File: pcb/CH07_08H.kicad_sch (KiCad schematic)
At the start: 10 parts

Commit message: Corrections to the coax driver
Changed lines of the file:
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@@
     (effects (font (size 1.27 1.27)) (justify right))
   )
-  (symbol (lib_id "Transistor_BJT:BC856BS") (at 106.68 52.07 0) (mirror x)
+  (symbol (lib_id "Transistor_BJT:BC856BS") (at 106.68 52.07 0) (mirror x) (unit 1)
     (in_bom yes) (on_board yes)
     (property "Reference" "Q?" (id 0) (at 111.506 53.2384 0)
@@
     (pin "6")
   )
-  (symbol (lib_id "Transistor_BJT:BC856BS") (at 106.68 114.3 0) (mirror x)
+  (symbol (lib_id "Transistor_BJT:BC856BS") (at 106.68 114.3 0) (mirror x) (unit 1)
     (in_bom yes) (on_board yes)
     (property "Reference" "Q?" (id 0) (at 111.506 115.4684 0)
@@
       (effects (font (size 1.27 1.27)) hide)
     )
-    (pin "3")
-    (pin "4")
-    (pin "5")
+    (pin "1")
+    (pin "2")
+    (pin "6")
   )
-  (symbol (lib_id "Device:R") (at 115.57 69.85 0)
+  (symbol (lib_id "Device:R") (at 115.57 69.85 0) (unit 1)
     (in_bom yes) (on_board yes)
     (property "Reference" "R?" (id 0) (at 117.348 68.6816 0)
@@
     (pin "2")
   )
-  (symbol (lib_id "power:GND") (at 115.57 86.36 0)
+  (symbol (lib_id "power:GND") (at 115.57 86.36 0) (unit 1)
     (in_bom yes) (on_board yes)
     (property "Reference" "#PWR?" (id 0) (at 115.57 92.71 0)
@@
     (pin "1")
   )
-  (symbol (lib_id "Device:R") (at 115.57 80.01 0)
+  (symbol (lib_id "Device:R") (at 115.57 80.01 0) (unit 1)
     (in_bom yes) (on_board yes)
     (property "Reference" "R?" (id 0) (at 117.348 78.8416 0)
@@
     (pin "2")
   )
-  (symbol (lib_id "Device:R") (at 114.3 132.08 0)
+  (symbol (lib_id "Device:R") (at 114.3 132.08 0) (unit 1)
     (in_bom yes) (on_board yes)
     (property "Reference" "R?" (id 0) (at 116.078 130.9116 0)
@@
     (pin "2")
   )
-  (symbol (lib_id "power:GND") (at 114.3 149.86 0)
+  (symbol (lib_id "power:GND") (at 114.3 149.86 0) (unit 1)
     (in_bom yes) (on_board yes)
     (property "Reference" "#PWR?" (id 0) (at 114.3 156.21 0)
@@
     (pin "1")
   )
-  (symbol (lib_id "Device:R") (at 114.3 143.51 0)
+  (symbol (lib_id "Device:R") (at 114.3 143.51 0) (unit 1)
     (in_bom yes) (on_board yes)
     (property "Reference" "R?" (id 0) (at 116.078 142.3416 0)
@@
     (pin "2")
   )
-  (symbol (lib_id "Connector:Conn_Coaxial") (at 115.57 59.69 0)
+  (symbol (lib_id "Connector:Conn_Coaxial") (at 115.57 59.69 0) (unit 1)
     (in_bom yes) (on_board yes)
     (property "Reference" "J?" (id 0) (at 118.11 60.325 0)
@@
     (pin "2")
   )
-  (symbol (lib_id "Device:R") (at 93.98 52.07 270)
+  (symbol (lib_id "Device:R") (at 93.98 52.07 270) (unit 1)
     (in_bom yes) (on_board yes)
     (property "Reference" "R?" (id 0) (at 93.98 46.8122 90))
@@
     (pin "2")
   )
-  (symbol (lib_id "Connector:Conn_Coaxial") (at 114.3 121.92 0)
+  (symbol (lib_id "Connector:Conn_Coaxial") (at 114.3 121.92 0) (unit 1)
     (in_bom yes) (on_board yes)
     (property "Reference" "J?" (id 0) (at 116.84 122.555 0)
@@
     (pin "2")
   )
-  (symbol (lib_id "Device:R") (at 93.98 114.3 270)
+  (symbol (lib_id "Device:R") (at 93.98 114.3 270) (unit 1)
     (in_bom yes) (on_board yes)
     (property "Reference" "R?" (id 0) (at 93.98 109.0422 90))

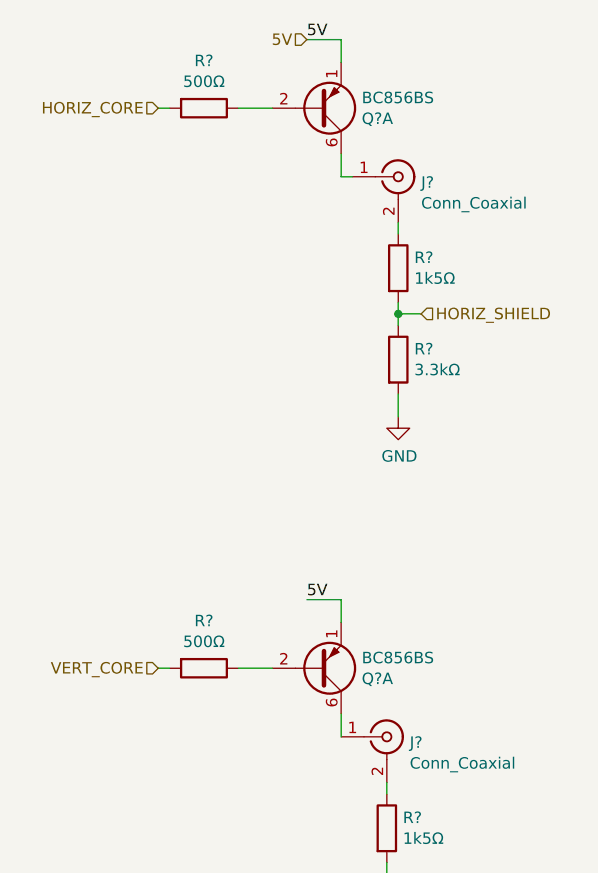
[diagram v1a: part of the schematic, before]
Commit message: Shift register updates - changes the driver from pnp to npn
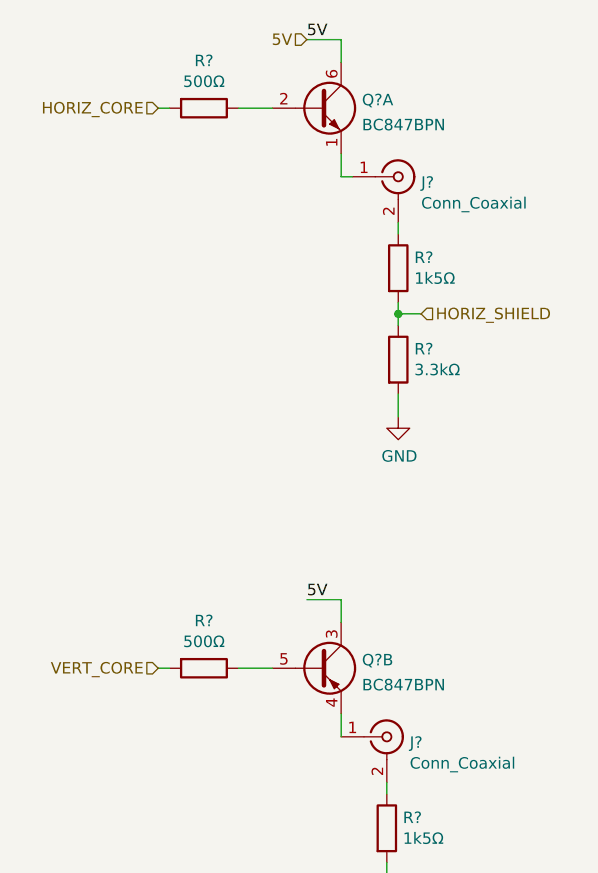
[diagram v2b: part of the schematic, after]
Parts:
- removed Q? (x2): BC856BS, Package_TO_SOT_SMD:SOT-363_SC-70-6, symbol Transistor_BJT:BC856BS
- added Q? (x2): BC847BPN, Package_TO_SOT_SMD:SOT-363_SC-70-6, symbol Transistor_BJT:BC847BPN
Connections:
- net 5V: now also Q?.3 (C2), Q?.6 (C1)
- net at R?.1: now also Q?.2 (B1)
- net at J?.1 (In): now also Q?.1 (E1)
- net at R?.1: now also Q?.5 (B2)
- net at J?.1 (In): now also Q?.4 (E2)
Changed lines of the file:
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@@
     (effects (font (size 1.27 1.27)) (justify right))
-  )
-  (symbol (lib_id "Transistor_BJT:BC856BS") (at 106.68 52.07 0) (mirror x) (unit 1)
-    (in_bom yes) (on_board yes)
-    (property "Reference" "Q?" (id 0) (at 111.506 53.2384 0)
-      (effects (font (size 1.27 1.27)) (justify left))
-    )
-    (property "Value" "BC856BS" (id 1) (at 111.506 50.927 0)
-      (effects (font (size 1.27 1.27)) (justify left))
-    )
-    (property "Footprint" "Package_TO_SOT_SMD:SOT-363_SC-70-6" (id 2) (at 111.76 54.61 0)
-      (effects (font (size 1.27 1.27)) hide)
-    )
-    (property "Datasheet" "https://assets.nexperia.com/documents/data-sheet/BC856BS.pdf" (id 3) (at 106.68 52.07 0)
-      (effects (font (size 1.27 1.27)) hide)
-    )
-    (pin "1")
-    (pin "2")
-    (pin "6")
-  )
-  (symbol (lib_id "Transistor_BJT:BC856BS") (at 106.68 114.3 0) (mirror x) (unit 1)
-    (in_bom yes) (on_board yes)
-    (property "Reference" "Q?" (id 0) (at 111.506 115.4684 0)
-      (effects (font (size 1.27 1.27)) (justify left))
-    )
-    (property "Value" "BC856BS" (id 1) (at 111.506 113.157 0)
-      (effects (font (size 1.27 1.27)) (justify left))
-    )
-    (property "Footprint" "Package_TO_SOT_SMD:SOT-363_SC-70-6" (id 2) (at 111.76 116.84 0)
-      (effects (font (size 1.27 1.27)) hide)
-    )
-    (property "Datasheet" "https://assets.nexperia.com/documents/data-sheet/BC856BS.pdf" (id 3) (at 106.68 114.3 0)
-      (effects (font (size 1.27 1.27)) hide)
-    )
-    (pin "1")
-    (pin "2")
-    (pin "6")
   )
   (symbol (lib_id "Device:R") (at 115.57 69.85 0) (unit 1)
@@
     (pin "2")
   )
+  (symbol (lib_id "Transistor_BJT:BC847BPN") (at 106.68 114.3 0) (unit 2)
+    (in_bom yes) (on_board yes) (fields_autoplaced)
+    (property "Reference" "Q?" (id 0) (at 111.5314 113.3915 0)
+      (effects (font (size 1.27 1.27)) (justify left))
+    )
+    (property "Value" "BC847BPN" (id 1) (at 111.5314 116.1666 0)
+      (effects (font (size 1.27 1.27)) (justify left))
+    )
+    (property "Footprint" "Package_TO_SOT_SMD:SOT-363_SC-70-6" (id 2) (at 111.76 111.76 0)
+      (effects (font (size 1.27 1.27)) hide)
+    )
+    (property "Datasheet" "https://assets.nexperia.com/documents/data-sheet/BC847BPN.pdf" (id 3) (at 106.68 114.3 0)
+      (effects (font (size 1.27 1.27)) hide)
+    )
+    (pin "3")
+    (pin "4")
+    (pin "5")
+  )
+  (symbol (lib_id "Transistor_BJT:BC847BPN") (at 106.68 52.07 0) (unit 1)
+    (in_bom yes) (on_board yes) (fields_autoplaced)
+    (property "Reference" "Q?" (id 0) (at 111.5314 51.1615 0)
+      (effects (font (size 1.27 1.27)) (justify left))
+    )
+    (property "Value" "BC847BPN" (id 1) (at 111.5314 53.9366 0)
+      (effects (font (size 1.27 1.27)) (justify left))
+    )
+    (property "Footprint" "Package_TO_SOT_SMD:SOT-363_SC-70-6" (id 2) (at 111.76 49.53 0)
+      (effects (font (size 1.27 1.27)) hide)
+    )
+    (property "Datasheet" "https://assets.nexperia.com/documents/data-sheet/BC847BPN.pdf" (id 3) (at 106.68 52.07 0)
+      (effects (font (size 1.27 1.27)) hide)
+    )
+    (pin "1")
+    (pin "2")
+    (pin "6")
+  )
 )

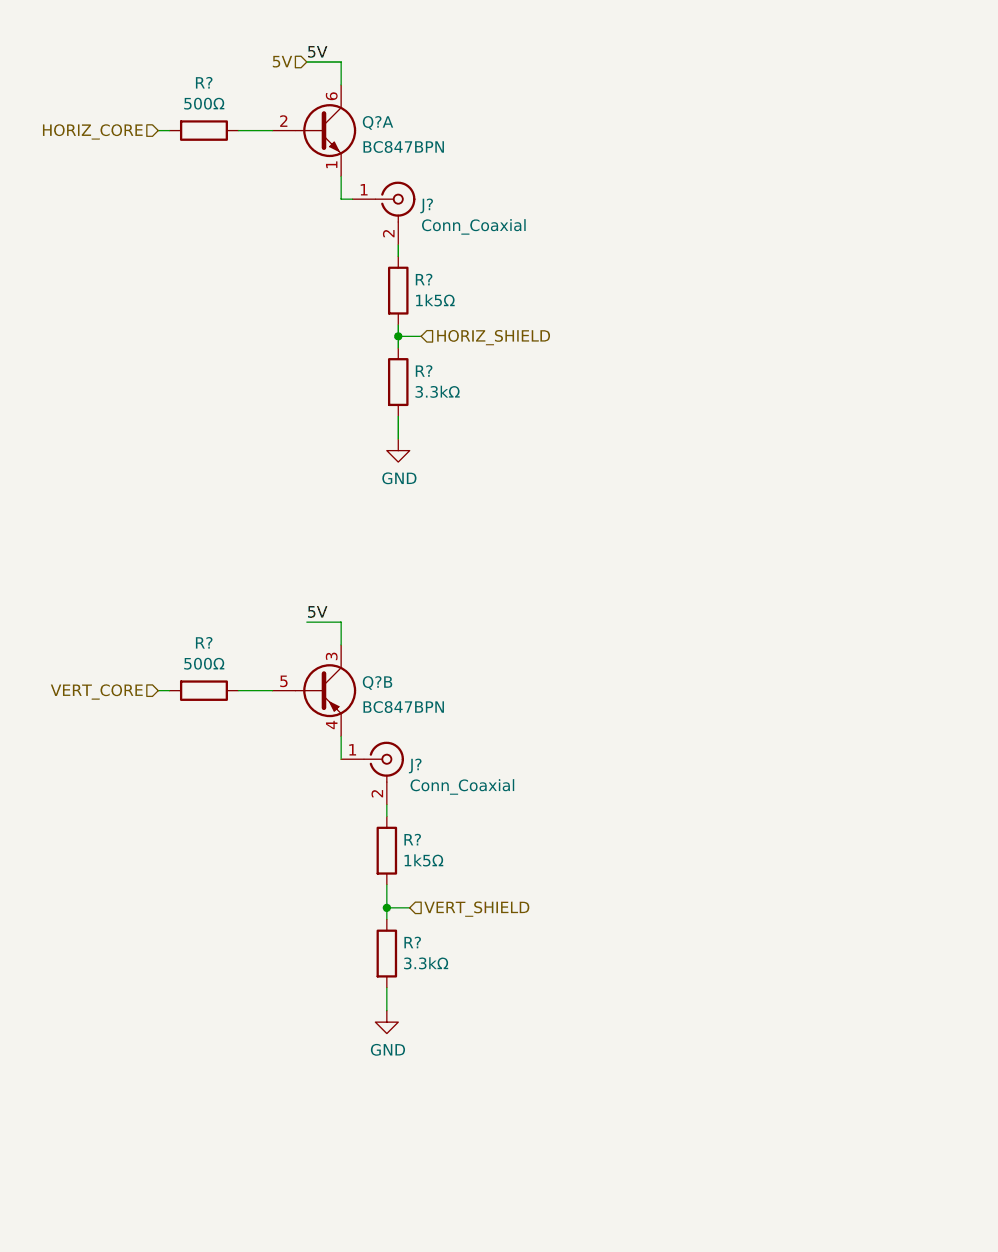
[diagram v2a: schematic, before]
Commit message: Adds line protection
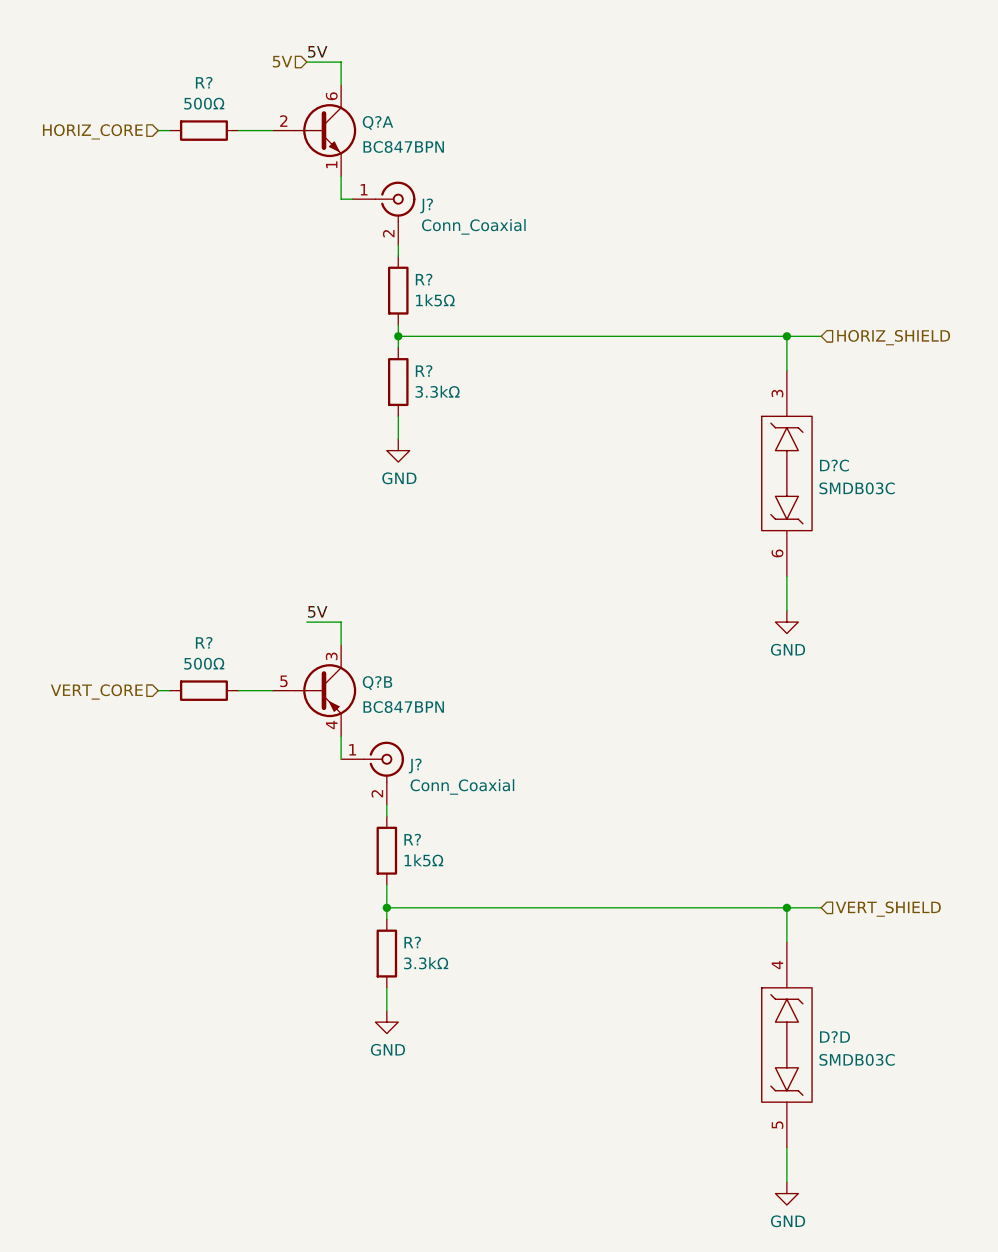
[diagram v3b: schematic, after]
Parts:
- added D? (x2): SMDB03C, Package_SO:SO-8_3.9x4.9mm_P1.27mm, symbol CoaxTester:SMDB03C
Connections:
- net GND: now also D?.5, D?.6
- net HORIZ_SHIELD: now also D?.3
- net VERT_SHIELD: now also D?.4
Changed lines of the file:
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@@
 (kicad_sch (version 20211123) (generator eeschema)
   (paper "A4")
+  (junction (at 158.75 74.93) (diameter 0) (color 0 0 0 0)
+  )
   (junction (at 114.3 138.43) (diameter 0) (color 0 0 0 0)
   )
   (junction (at 115.57 74.93) (diameter 0) (color 0 0 0 0)
   )
+  (junction (at 158.75 138.43) (diameter 0) (color 0 0 0 0)
+  )
   (wire (pts (xy 109.22 119.38) (xy 109.22 121.92))
     (stroke (width 0) (type default) (color 0 0 0 0))
   )
+  (wire (pts (xy 158.75 165.1) (xy 158.75 168.91))
+    (stroke (width 0) (type default) (color 0 0 0 0))
+  )
+  (wire (pts (xy 158.75 101.6) (xy 158.75 105.41))
+    (stroke (width 0) (type default) (color 0 0 0 0))
+  )
+  (wire (pts (xy 158.75 138.43) (xy 158.75 142.24))
+    (stroke (width 0) (type default) (color 0 0 0 0))
+  )
   (wire (pts (xy 109.22 46.99) (xy 109.22 44.45))
     (stroke (width 0) (type default) (color 0 0 0 0))
   )
-  (wire (pts (xy 115.57 74.93) (xy 118.11 74.93))
+  (wire (pts (xy 115.57 74.93) (xy 158.75 74.93))
     (stroke (width 0) (type default) (color 0 0 0 0))
   )
@@
     (stroke (width 0) (type default) (color 0 0 0 0))
   )
+  (wire (pts (xy 158.75 74.93) (xy 158.75 78.74))
+    (stroke (width 0) (type default) (color 0 0 0 0))
+  )
   (wire (pts (xy 114.3 127) (xy 114.3 128.27))
     (stroke (width 0) (type default) (color 0 0 0 0))
@@
     (stroke (width 0) (type default) (color 0 0 0 0))
   )
+  (wire (pts (xy 158.75 74.93) (xy 162.56 74.93))
+    (stroke (width 0) (type default) (color 0 0 0 0))
+  )
   (wire (pts (xy 114.3 147.32) (xy 114.3 149.86))
     (stroke (width 0) (type default) (color 0 0 0 0))
@@
     (stroke (width 0) (type default) (color 0 0 0 0))
   )
+  (wire (pts (xy 158.75 138.43) (xy 162.56 138.43))
+    (stroke (width 0) (type default) (color 0 0 0 0))
+  )
   (wire (pts (xy 109.22 57.15) (xy 109.22 59.69))
     (stroke (width 0) (type default) (color 0 0 0 0))
@@
     (stroke (width 0) (type default) (color 0 0 0 0))
   )
-  (wire (pts (xy 114.3 138.43) (xy 116.84 138.43))
+  (wire (pts (xy 114.3 138.43) (xy 158.75 138.43))
     (stroke (width 0) (type default) (color 0 0 0 0))
   )
@@
     (effects (font (size 1.27 1.27)) (justify right))
   )
-  (hierarchical_label "HORIZ_SHIELD" (shape input) (at 118.11 74.93 0)
+  (hierarchical_label "HORIZ_SHIELD" (shape input) (at 162.56 74.93 0)
     (effects (font (size 1.27 1.27)) (justify left))
   )
-  (hierarchical_label "VERT_SHIELD" (shape input) (at 116.84 138.43 0)
+  (hierarchical_label "VERT_SHIELD" (shape input) (at 162.56 138.43 0)
     (effects (font (size 1.27 1.27)) (justify left))
   )
@@
     (pin "2")
   )
+  (symbol (lib_id "power:GND") (at 158.75 168.91 0) (unit 1)
+    (in_bom yes) (on_board yes)
+    (property "Reference" "#PWR?" (id 0) (at 158.75 175.26 0)
+      (effects (font (size 1.27 1.27)) hide)
+    )
+    (property "Value" "GND" (id 1) (at 158.877 173.3042 0))
+    (property "Footprint" "" (id 2) (at 158.75 168.91 0)
+      (effects (font (size 1.27 1.27)) hide)
+    )
+    (property "Datasheet" "" (id 3) (at 158.75 168.91 0)
+      (effects (font (size 1.27 1.27)) hide)
+    )
+    (pin "1")
+  )
+  (symbol (lib_id "CoaxTester:SMDB03C") (at 158.75 153.67 0) (unit 4)
+    (in_bom yes) (on_board yes) (fields_autoplaced)
+    (property "Reference" "D?" (id 0) (at 162.2552 152.8353 0)
+      (effects (font (size 1.27 1.27)) (justify left))
+    )
+    (property "Value" "SMDB03C" (id 1) (at 162.2552 155.3722 0)
+      (effects (font (size 1.27 1.27)) (justify left))
+    )
+    (property "Footprint" "Package_SO:SO-8_3.9x4.9mm_P1.27mm" (id 2) (at 158.75 152.4 0)
+      (effects (font (size 1.27 1.27)) hide)
+    )
+    (property "Datasheet" "https://www.smc-diodes.com/propdf/SMDB03C%20THRU%20SMDB24C%20N0426%20REV.A.pdf" (id 3) (at 158.75 152.4 0)
+      (effects (font (size 1.27 1.27)) hide)
+    )
+    (pin "4")
+    (pin "5")
+  )
   (symbol (lib_id "Transistor_BJT:BC847BPN") (at 106.68 114.3 0) (unit 2)
     (in_bom yes) (on_board yes) (fields_autoplaced)
@@
     (pin "5")
   )
+  (symbol (lib_id "power:GND") (at 158.75 105.41 0) (unit 1)
+    (in_bom yes) (on_board yes)
+    (property "Reference" "#PWR?" (id 0) (at 158.75 111.76 0)
+      (effects (font (size 1.27 1.27)) hide)
+    )
+    (property "Value" "GND" (id 1) (at 158.877 109.8042 0))
+    (property "Footprint" "" (id 2) (at 158.75 105.41 0)
+      (effects (font (size 1.27 1.27)) hide)
+    )
+    (property "Datasheet" "" (id 3) (at 158.75 105.41 0)
+      (effects (font (size 1.27 1.27)) hide)
+    )
+    (pin "1")
+  )
   (symbol (lib_id "Transistor_BJT:BC847BPN") (at 106.68 52.07 0) (unit 1)
     (in_bom yes) (on_board yes) (fields_autoplaced)
@@
     (pin "6")
   )
+  (symbol (lib_id "CoaxTester:SMDB03C") (at 158.75 90.17 0) (unit 3)
+    (in_bom yes) (on_board yes) (fields_autoplaced)
+    (property "Reference" "D?" (id 0) (at 162.2552 89.3353 0)
+      (effects (font (size 1.27 1.27)) (justify left))
+    )
+    (property "Value" "SMDB03C" (id 1) (at 162.2552 91.8722 0)
+      (effects (font (size 1.27 1.27)) (justify left))
+    )
+    (property "Footprint" "Package_SO:SO-8_3.9x4.9mm_P1.27mm" (id 2) (at 158.75 88.9 0)
+      (effects (font (size 1.27 1.27)) hide)
+    )
+    (property "Datasheet" "https://www.smc-diodes.com/propdf/SMDB03C%20THRU%20SMDB24C%20N0426%20REV.A.pdf" (id 3) (at 158.75 88.9 0)
+      (effects (font (size 1.27 1.27)) hide)
+    )
+    (pin "3")
+    (pin "6")
+  )
